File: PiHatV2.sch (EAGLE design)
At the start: 29 parts, among them U1 RASPBERRY_PI_3_MODEL_B+, X2 SCREENBREAKOUT_SCREENBREAKOUT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

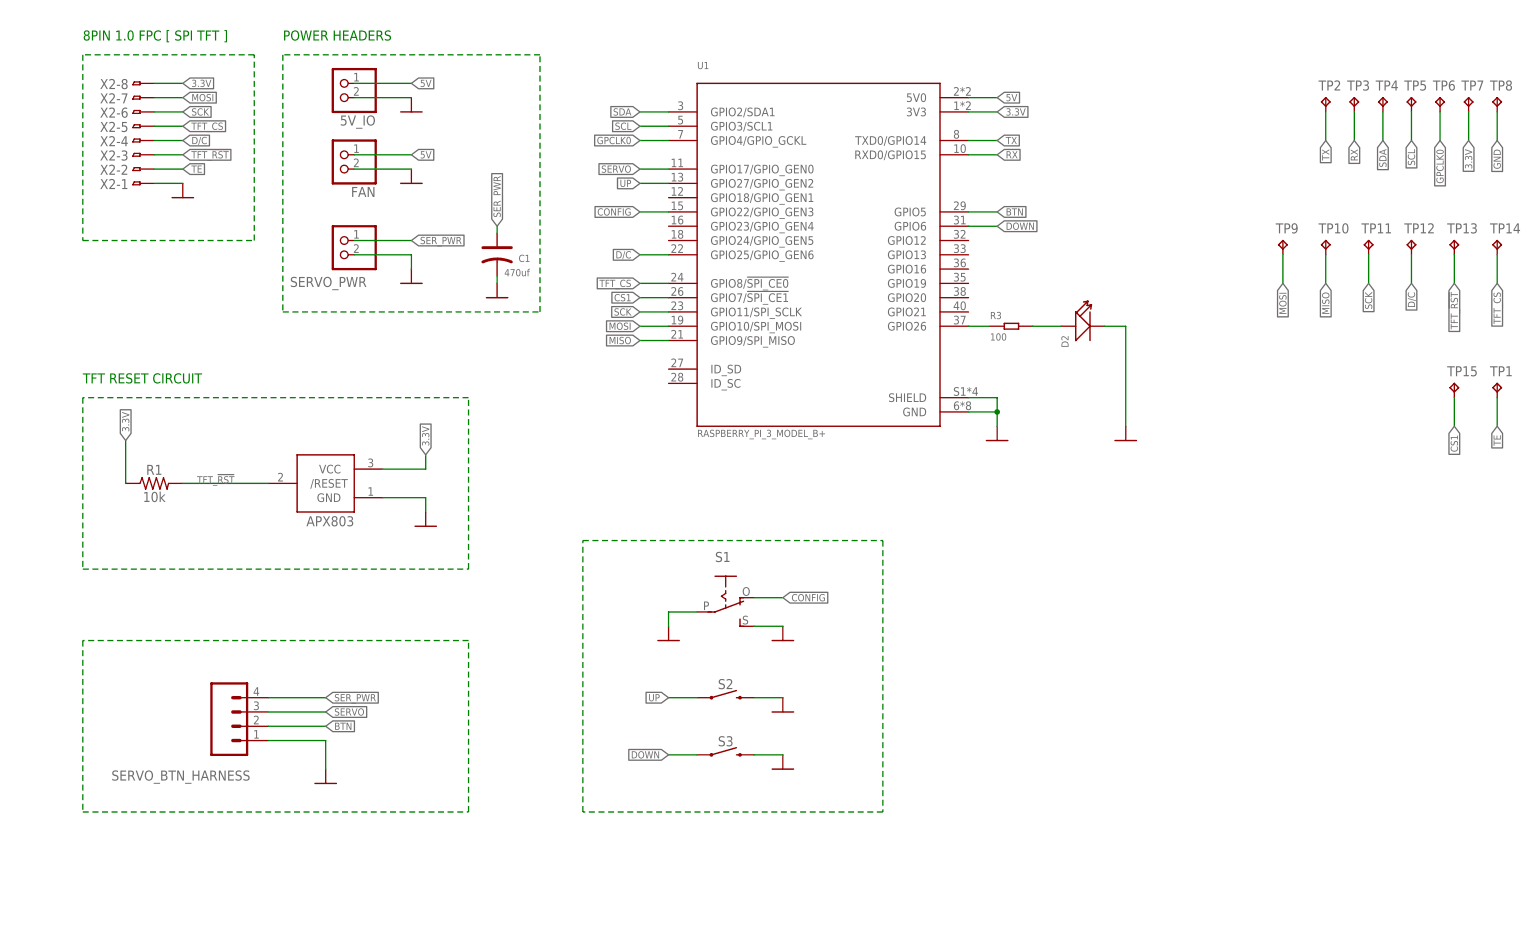
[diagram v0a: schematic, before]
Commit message: support for a limit switch button for cont servo
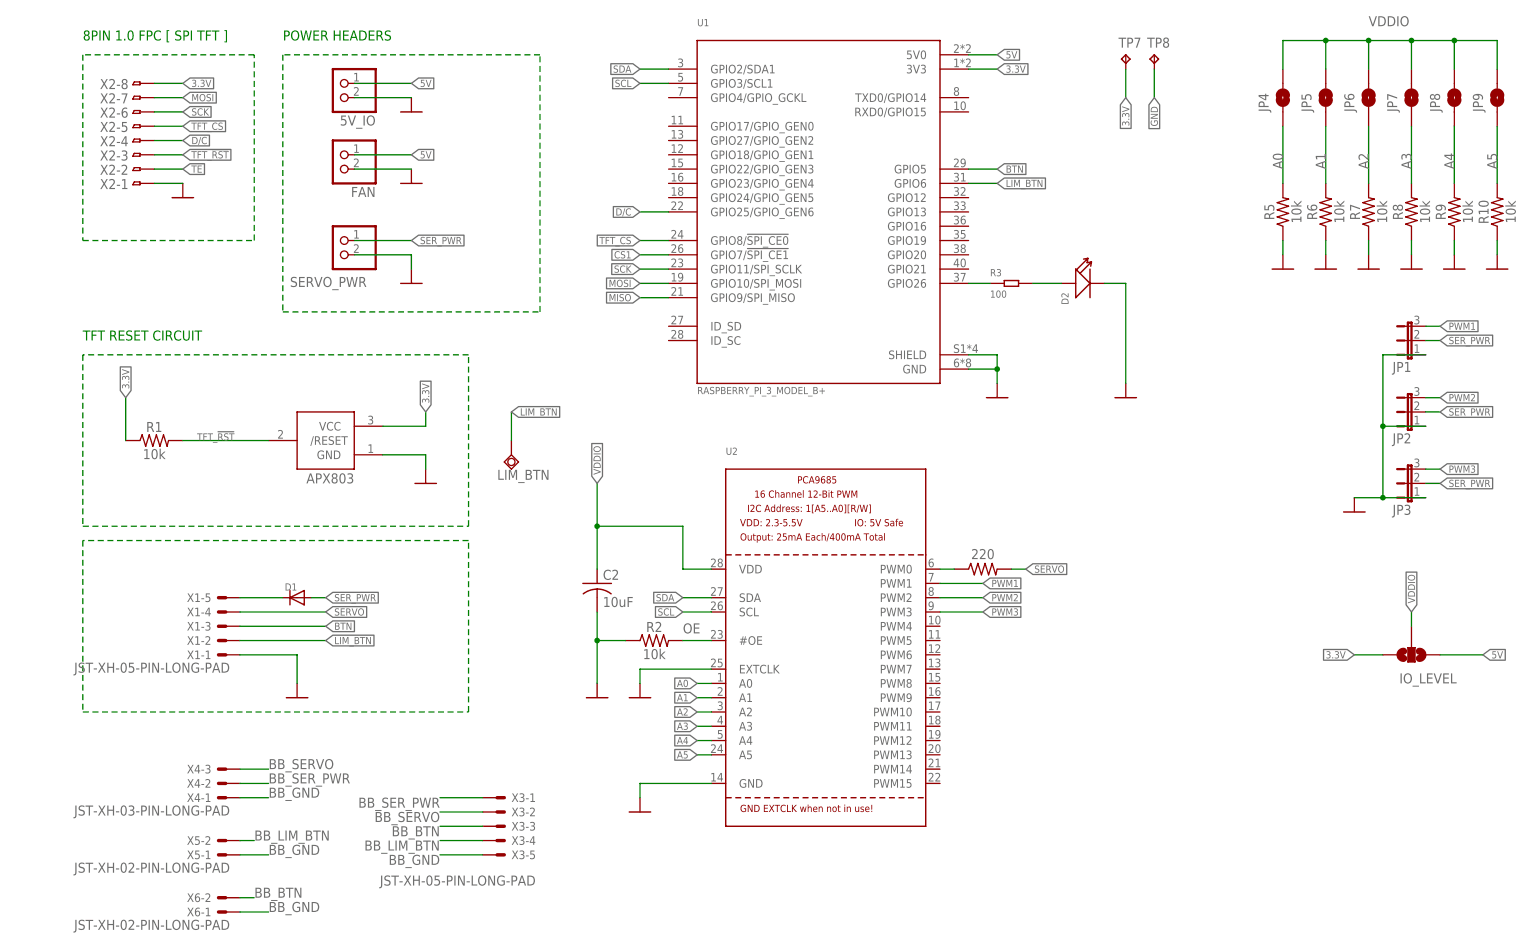
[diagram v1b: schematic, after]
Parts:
- removed C1: 470uf, Seeed-Capacitor:TANTALUM-SMD-470UF-6.3V(AVX-D)
- removed S1: (no value), adafruit:EG1218S
- removed S2, S3: SPARKFUN-SWITCHES_MOMENTARY-SWITCH-SPST-PTH-12MM, ARDUINO_3V_TTL_INTERFACE_2_PI:SPARKFUN-SWITCHES_MOMENTARY-SWITCH-SPST-PTH-12MM
- removed SERVO_BTN_HARNESS: (no value), SparkFun-Connectors:CONN_04JST-PTH
- removed TP1, TP10, TP11, TP12, TP13, TP14, TP15, TP2, TP3, TP4, TP5, TP6, TP9: TPB2,54, testpad:TPB2,54
- added C2: 10uF, adafruit:C-USC0805K
- added D1: (no value), adafruit:DIODESMA
- added IO_LEVEL: JUMPER-SMT_3_NO_NO-SILK, SparkFun-Jumpers:JUMPER-SMT_3_NO_NO-SILK
- added JP1, JP2, JP3: (no value), FeatherWing:LED-BADGE_SCHEMATIC_JUMPER_JP2E
- added JP4, JP5, JP6, JP7, JP8, JP9: JUMPER-SMT_2_NO_NO-SILK, SparkFun-Jumpers:JUMPER-SMT_2_NO_NO-SILK
- added LIM_BTN: TESTPAD_TPSQB1,27, ARDUINO_3V_TTL_INTERFACE_2_PI:TESTPAD_TPSQB1,27
- added R10, R2, R5, R6, R7, R8, R9: 10k, PiHat:ARDUINO_3V_TTL_INTERFACE_2_PI_SPARKFUN-RESISTORS_10KOHM-0603-1/10W-1%
- added R4: 220, PiHat:ARDUINO_3V_TTL_INTERFACE_2_PI_SPARKFUN-RESISTORS_10KOHM-0603-1/10W-1%
- added U2: (no value), adafruit:PCA9685
- added X1, X3: JST-XH-05-PIN-LONG-PAD, Rembrandt Electronics - JST XH Connectors v1-0:JST-XH-05-PIN-LONG-PAD
- added X4: JST-XH-03-PIN-LONG-PAD, Rembrandt Electronics - JST XH Connectors v1-0:JST-XH-03-PIN-LONG-PAD
- added X5, X6: JST-XH-02-PIN-LONG-PAD, Rembrandt Electronics - JST XH Connectors v1-0:JST-XH-02-PIN-LONG-PAD
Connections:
- removed net CONFIG: S1.O, U1.GPIO22/GPIO_GEN3
- removed net DOWN: S3.1, U1.GPIO6
- removed net GPCLK0: TP6.TP, U1.GPIO4/GPIO_GCKL
- removed net RX: TP3.TP, U1.RXD0/GPIO15
- removed net TX: TP2.TP, U1.TXD0/GPIO14
- removed net UP: S2.1, U1.GPIO27/GPIO_GEN2
- new net A0: JP4.1, R5.2, U2.A0
- new net A1: JP5.1, R6.2, U2.A1
- new net A2: JP6.1, R7.2, U2.A2
- new net A3: JP7.1, R8.2, U2.A3
- new net A4: JP8.1, R9.2, U2.A4
- new net A5: JP9.1, R10.2, U2.A5
- new net BB_BTN: X3-3.S, X6-2.S
- new net BB_GND: X3-5.S, X4-1.S, X5-1.S, X6-1.S
- new net BB_LIM_BTN: X3-4.S, X5-2.S
- new net BB_SERVO: X3-2.S, X4-3.S
- new net BB_SER_PWR: X3-1.S, X4-2.S
- new net LIM_BTN: LIM_BTN.TP, U1.GPIO6, X1-2.S
- new net N$5: R4.1, U2.PWM0
- new net N$6: D1.C, X1-5.S
- new net OE: R2.2, U2.#OE
- new net PWM1: JP1.3, U2.PWM1
- new net PWM2: JP2.3, U2.PWM2
- new net PWM3: JP3.3, U2.PWM3
- new net VDDIO: C2.1, IO_LEVEL.2, JP4.2, JP5.2, JP6.2, JP7.2, JP8.2, JP9.2, U2.VDD
- net 3.3V: now also IO_LEVEL.3
- net 5V: now also IO_LEVEL.1
- net BTN: now also X1-3.S; no longer SERVO_BTN_HARNESS.2
- net CS1: no longer TP15.TP
- net D/C: no longer TP12.TP
- net GND: now also C2.2, JP1.1, JP2.1, JP3.1, R10.1, R2.1, R5.1, R6.1, R7.1, R8.1, R9.1, U2.EXTCLK, U2.GND, X1-1.S; no longer C1.-, S1.P, S1.S, S2.2, S3.2, SERVO_BTN_HARNESS.1
- net MISO: no longer TP10.TP
- net MOSI: no longer TP9.TP
- net SCK: no longer TP11.TP
- net SCL: now also U2.SCL; no longer TP5.TP
- net SDA: now also U2.SDA; no longer TP4.TP
- net SERVO: now also R4.2, X1-4.S; no longer SERVO_BTN_HARNESS.3, U1.GPIO17/GPIO_GEN0
- net SER_PWR: now also D1.A, JP1.2, JP2.2, JP3.2; no longer C1.+, SERVO_BTN_HARNESS.4
- net TE: no longer TP1.TP
- net TFT_!RST: no longer TP13.TP
- net TFT_CS: no longer TP14.TP
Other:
- moved on the sheet: APX803, D2, R1, R3, TP7, TP8, U1
